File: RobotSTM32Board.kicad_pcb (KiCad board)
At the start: 2 copper layers, 70 x 88.6 mm, 86 parts, among them IC1 TB6612FNG, IC2 TB6612FNG, J1 MotorA, J10 Qwiik1, J11 Qwiik2, J12 Qwiik3, J13 Qwiik4, J14 Qwiik5, J15 39-30-0040, J15 DCIn, J16 UJC-H-G-SMT-2-P6-TR, J2 MotorB, J3 MotorC, J4 MotorD, J5 EncoderA, J6 EncoderB, J7 EncoderC, J8 EncoderD, J9 ESTOP, Q1 NPN, Q2 NMOS_Substrate, Q3 NMOS_Substrate, U1 NUCLEO-F411RE, U3 TPS564252DRLR, U4 TPS51386RJNR, U5 LM27403SQ/NOPB

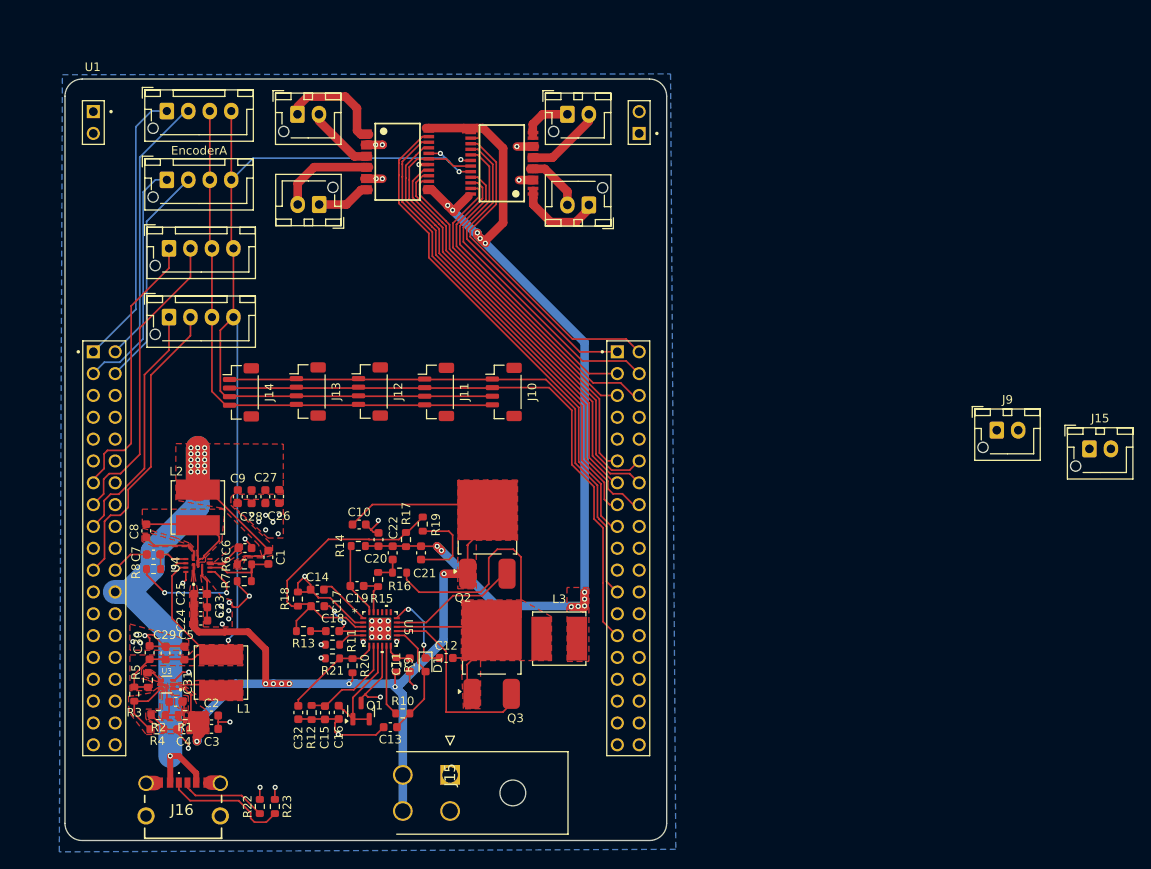
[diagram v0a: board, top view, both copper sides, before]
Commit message: Added battery connectors
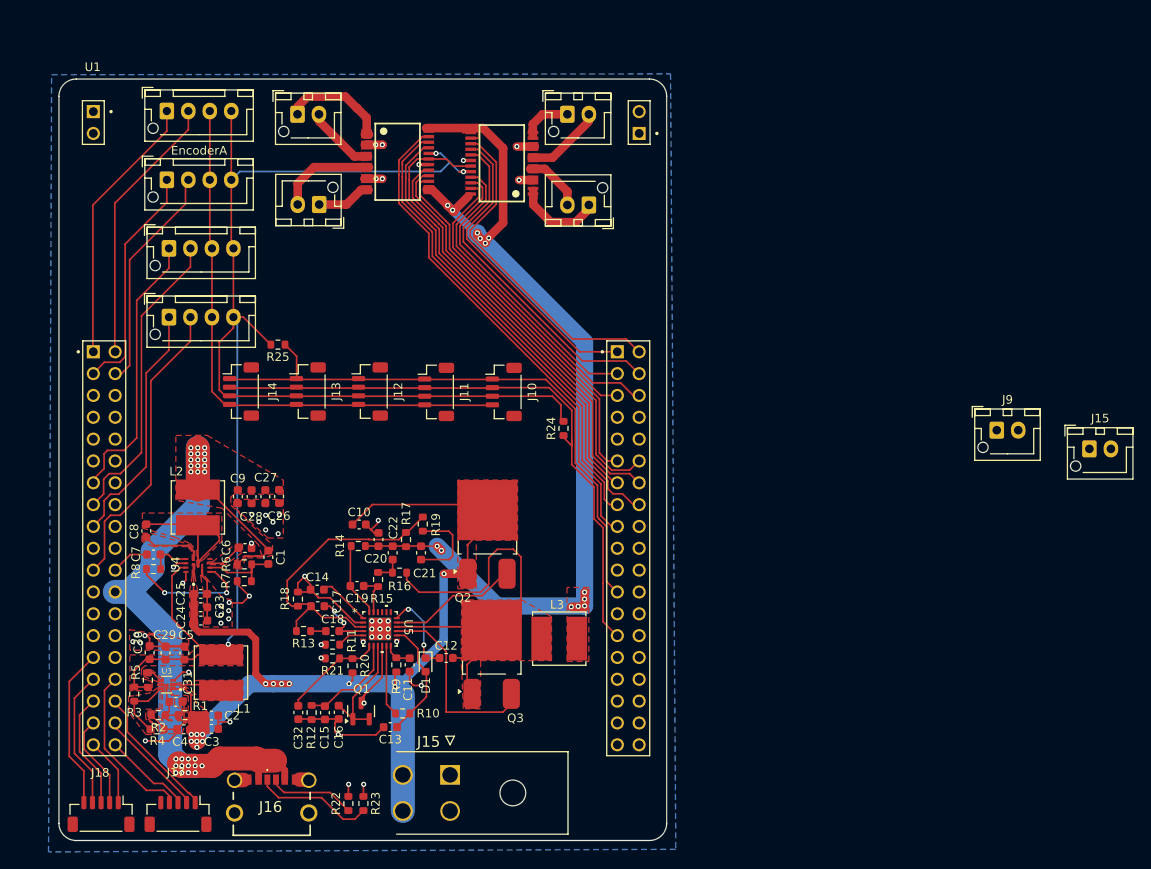
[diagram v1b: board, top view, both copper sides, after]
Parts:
- added J17: BatteryOutputs, Connector_JST:JST_SH_BM05B-SRSS-TB_1x05-1MP_P1.00mm_Vertical, F.Cu at (121.7, 137.8)
- added J18: BatteryInputs, Connector_JST:JST_SH_BM05B-SRSS-TB_1x05-1MP_P1.00mm_Vertical, F.Cu at (112.7, 137.8)
- added R24: 10k, Resistor_SMD:R_0603_1608Metric, F.Cu at (166.5, 92.9)
- added R25: 10k, Resistor_SMD:R_0603_1608Metric, F.Cu at (133.3, 83.2)
- moved J16 10.3 mm to (132.6, 136.8)
- moved R22 10.3 mm to (141.5, 136.5)
- moved R23 10.3 mm to (143.2, 136.5)
- moved J14 0.10 mm to (129.0, 88.6)
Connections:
- U1 pad CN7_29: unconnected-(U1A-PH0-PadCN7_29) -> USB_C_Interrupt
- U1 pad CN7_31: unconnected-(U1A-PH1-PadCN7_31) -> MCU_CHARGE_EN
- U1 pad CN7_32: unconnected-(U1A-PA4-PadCN7_32) -> ALERT
- U1 pad CN7_33: unconnected-(U1A-VBAT-PadCN7_33) -> MCU_USB_DETECT
- U1 pad CN7_34: unconnected-(U1A-PB0-PadCN7_34) -> ADC1_MCU
- U1 pad CN7_35: unconnected-(U1A-PC2-PadCN7_35) -> MCU_DISCHRG_CTRL
- U1 pad CN7_36: unconnected-(U1A-PC1-PadCN7_36) -> ADC2_MCU
- U1 pad CN7_37: unconnected-(U1A-PC3-PadCN7_37) -> MCU_CHRG_CTRL
- U1 pad CN7_38: unconnected-(U1A-PC0-PadCN7_38) -> ADC3_MCU
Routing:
- net ALERT: track 0.00 -> 19.2 mm
- net USB_C_Interrupt: track 0.00 -> 18.7 mm
- net 3V3: track 166.9 -> 183.6 mm
- net MCU_CHARGE_EN: track 0.00 -> 16.1 mm
- net ADC1_MCU: track 0.00 -> 15.7 mm
- net MCU_USB_DETECT: track 0.00 -> 13.5 mm
- net 5V: track 72.7 -> 85.9 mm, vias 16 -> 28
- net ADC2_MCU: track 0.00 -> 12.7 mm
- net MCU_DISCHRG_CTRL: track 0.00 -> 10.9 mm
- net ADC3_MCU: track 0.00 -> 10.4 mm
- net MCU_CHRG_CTRL: track 0.00 -> 7.93 mm
- net SCL: track 64.9 -> 69.5 mm
- net SDA: track 69.3 -> 71.6 mm
- net Vin: track 136.3 -> 135.3 mm, vias 8 -> 14
- net EncoderA1: track 32.6 -> 31.7 mm
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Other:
- board size 70 x 88.6 mm -> 70.7 x 88.6 mm

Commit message: added fuse
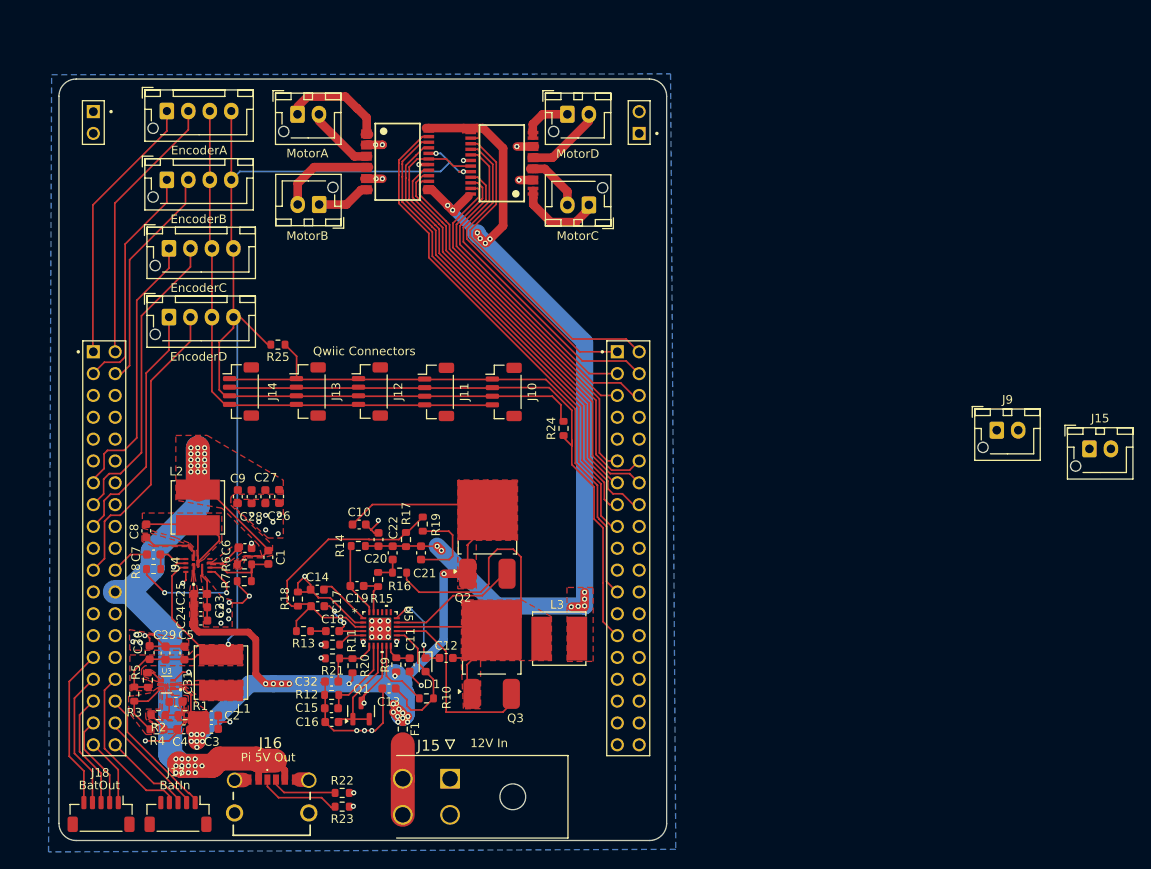
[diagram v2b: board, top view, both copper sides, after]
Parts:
- added F1: 5A, Resistor_SMD:R_0603_1608Metric, F.Cu at (147.8, 127.9)
- moved C32 5.29 mm to (139.5, 122.3), turned to 180 degrees
- moved C13 4.50 mm to (146.2, 123.2)
- moved R10 3.26 mm to (150.6, 124.3)
- moved R12 3.10 mm to (139.5, 123.9), turned to 180 degrees
- moved R23 2.50 mm to (140.8, 136.9), turned to 0 degrees
- moved R22 1.43 mm to (140.8, 135.3), turned to 0 degrees
- moved C16 1.38 mm to (139.6, 127.0), turned to 180 degrees
- moved C15 0.92 mm to (139.5, 125.5), turned to 180 degrees
- moved J15 0.45 mm to (153.3, 133.7)
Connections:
- J15 pad 3: Vin -> +12V
- J15 pad 4: Vin -> +12V
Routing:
- net +12V: track 0.00 -> 8.21 mm
- net Net-(U5-UVLO/EN): track 11.9 -> 7.10 mm
- net Net-(J16-CC1): track 14.0 -> 9.73 mm
- net Vin: track 135.3 -> 132.1 mm, vias 14 -> 23
- net Net-(J16-CC2): track 9.68 -> 7.28 mm
- net Net-(U5-OTP): track 11.8 -> 9.55 mm
- net Net-(D1-A): track 14.2 -> 16.2 mm
- net GND: track 175.9 -> 176.3 mm, vias 52 -> 54
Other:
- board text added: "12V In"
- board text added: "BatIn"
- board text added: "BatOut"
- board text added: "EncoderB"
- board text added: "EncoderC"
- board text added: "EncoderD"
- board text added: "MotorA"
- board text added: "MotorB"
- board text added: "MotorC"
- board text added: "MotorD"
- board text added: "Pi 5V Out"
- board text added: "Qwiic Connectors"

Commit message: commit of the finished thing before i tidy it up for the report
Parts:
- removed J14: Qwiik5, Connector_JST:JST_SH_BM04B-SRSS-TB_1x04-1MP_P1.00mm_Vertical
- added H1: MountingHole, MountingHole:MountingHole_2.5mm, F.Cu at (140.0, 70.0)
- added H2: MountingHole, MountingHole:MountingHole_2.5mm, F.Cu at (140.0, 90.0)
- added H3: MountingHole, MountingHole:MountingHole_2.5mm, F.Cu at (170.0, 70.0)
- added H4: MountingHole, MountingHole:MountingHole_2.5mm, F.Cu at (170.0, 130.0)
- moved J13 12.8 mm to (125.8, 82.0)
- moved J12 10.3 mm to (136.0, 82.0)
- moved J11 8.63 mm to (146.1, 82.1)
- moved ? 7.54 mm to (141.5, 109.6)
- moved C1 7.54 mm to (128.5, 101.3)
- moved C10 7.54 mm to (139.1, 97.5)
- moved C11 7.54 mm to (145.0, 113.8)
- moved C12 7.54 mm to (149.2, 113.0)
- moved C14 7.54 mm to (134.2, 105.1)
- moved C15 7.54 mm to (135.9, 118.9)
- moved C16 7.54 mm to (135.9, 120.5)
- moved C17 7.54 mm to (134.3, 107.0)
- moved C18 7.54 mm to (136.0, 109.9)
- moved C19 7.54 mm to (138.8, 104.6)
- moved C20 7.54 mm to (143.0, 100.8)
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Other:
- board text added: "I2C Expansion (Qwiic Connectors)"
- board text removed: "Qwiic Connectors"
